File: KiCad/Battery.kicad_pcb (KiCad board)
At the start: 2 copper layers, 19 x 29 mm, 26 parts, among them J1 Connector, J2 USB-C, J3 DC, Q1 RN1701, U1 ESP32-WROOM-32, U2 FT231XQ, U3 NX6020CAKS

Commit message: Tweak regulater
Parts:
- Reg1: footprint RevK:RegulatorBlock2 -> RevK:RegulatorBlock

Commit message: Tweak
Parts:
- moved R7 0.22 mm to (127.5, 110.4)

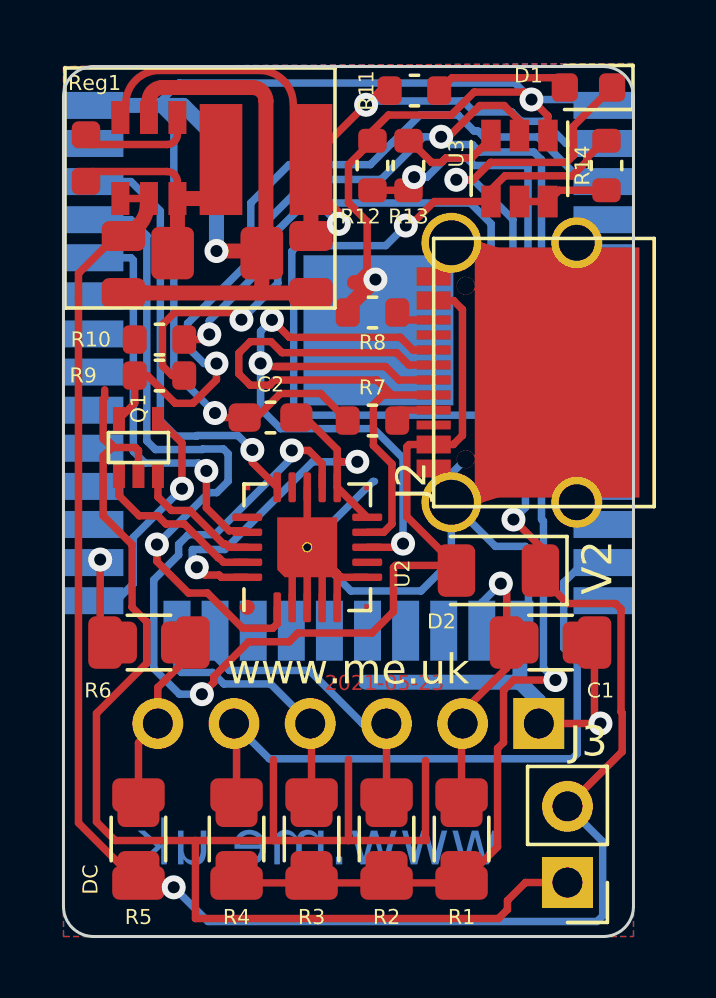
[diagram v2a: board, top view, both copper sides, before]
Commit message: Added BCD_Charger
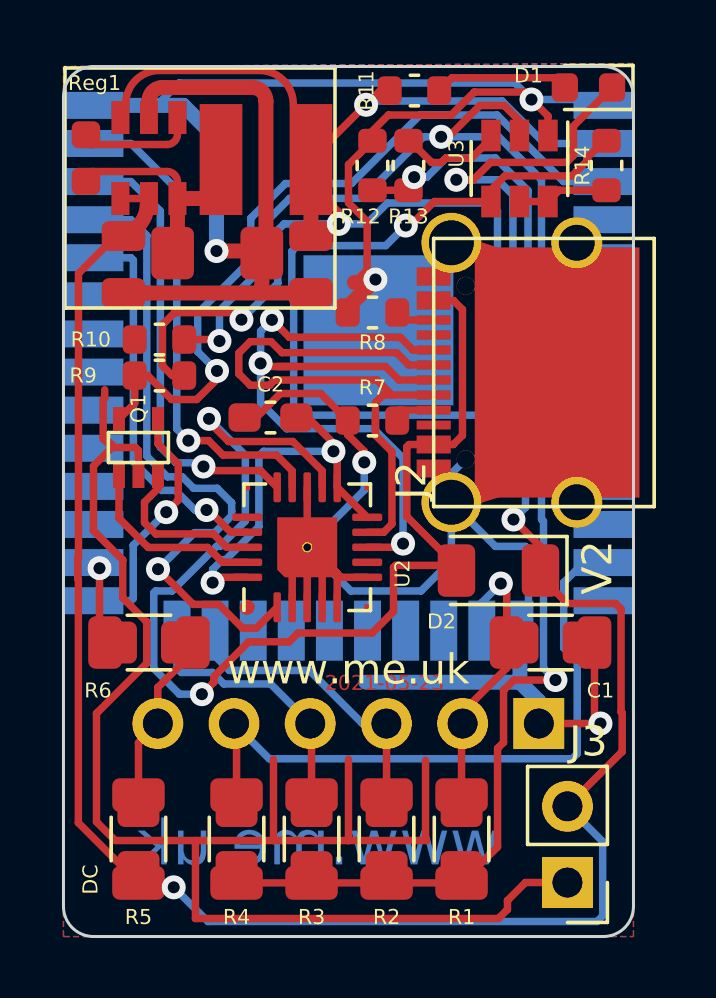
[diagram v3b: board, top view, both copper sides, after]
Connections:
- net CBUS renamed VBUS_SENSE
- U1 pad 37: Net-(U1-Pad37) -> BCD_CHARGER
- U2 pad 14: Net-(U2-Pad14) -> BCD_CHARGER
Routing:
- net BCD_CHARGER: track 0.00 -> 16.4 mm, vias 0 -> 1
- net GND: track 166.2 -> 156.4 mm
- net VBUS: track 37.2 -> 41.1 mm
- net USB3.3: track 14.8 -> 13.5 mm
- net GPIO0: track 4.37 -> 5.50 mm
- net +3V3: track 64.9 -> 63.9 mm
- net Net-(Q1-Pad5): track 26.4 -> 25.5 mm
- net I: track 13.4 -> 12.9 mm

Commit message: USB present is powered CBUS pin
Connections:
- net BCD_CHARGER renamed CHARGER
- net VBUS_SENSE renamed USB

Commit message: Update documentation
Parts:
- C2: footprint Capacitor_SMD:C_0603_1608Metric_Pad1.08x0.95mm_HandSolder -> RevK:C_0603
- moved R7 0.05 mm to (127.5, 110.3)
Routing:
- net GND: track 156.4 -> 158.6 mm
- net USB3.3: track 13.5 -> 12.4 mm
- net O: track 21.5 -> 22.3 mm
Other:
- board text added: "2021-05-25"
- board text added: "V3"
- board text removed: "V2"

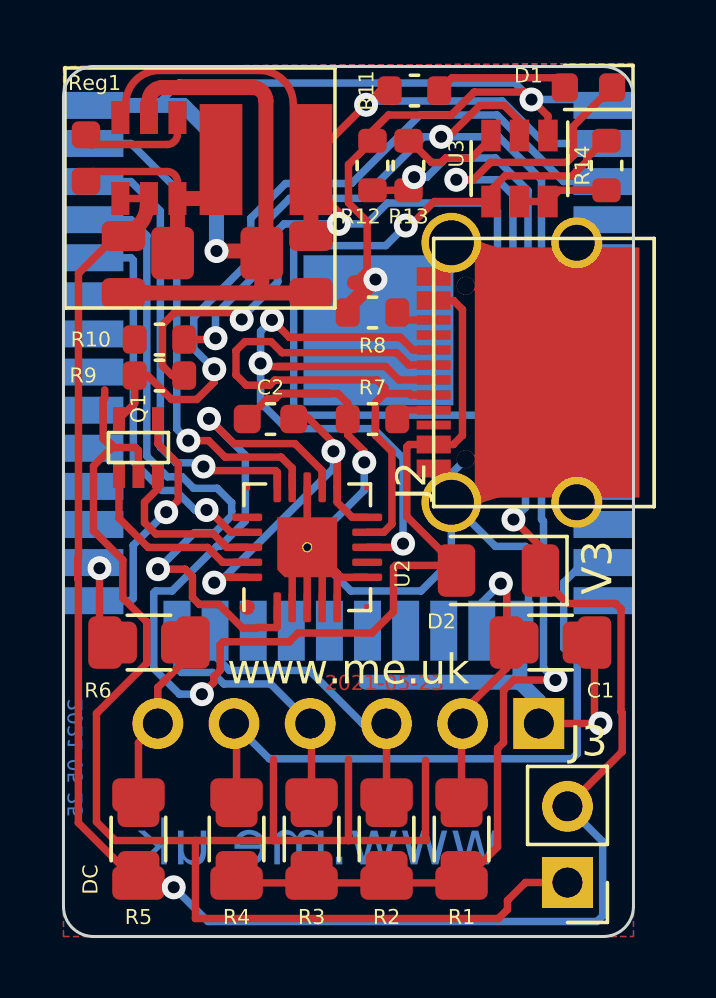
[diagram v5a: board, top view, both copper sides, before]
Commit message: Wrong footprint FFS
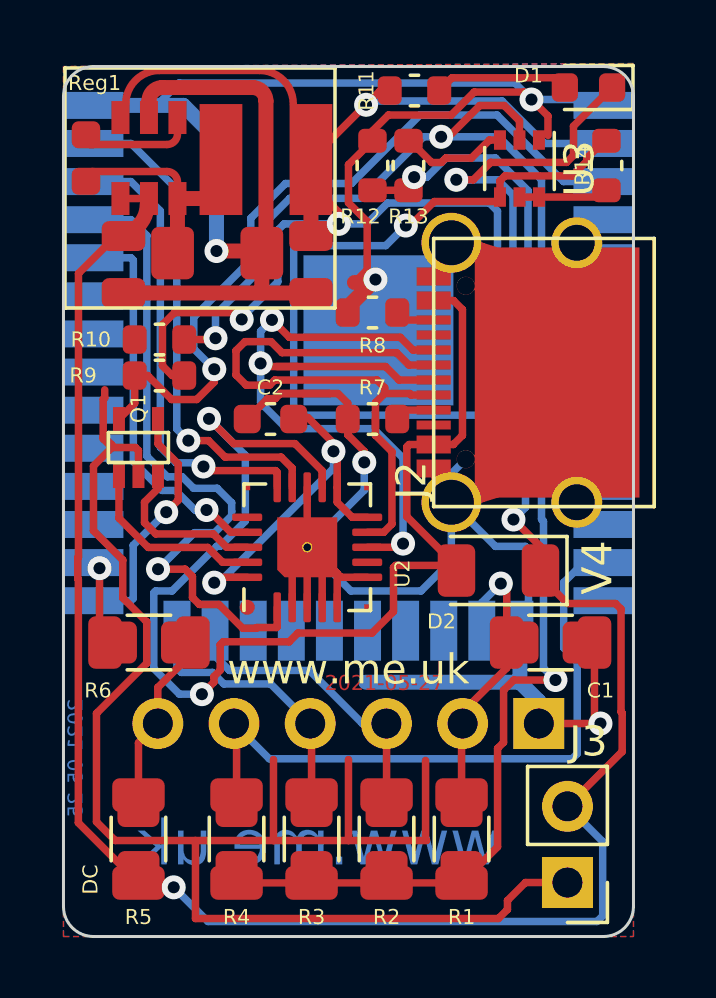
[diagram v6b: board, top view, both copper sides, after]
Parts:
- U3: footprint Package_TO_SOT_SMD:SOT-23-6 -> Package_TO_SOT_SMD:SOT-363_SC-70-6
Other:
- board text added: "2021-05-27"
- board text added: "V4"
- board text removed: "2021-05-23"
- board text removed: "V3"
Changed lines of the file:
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@@
     (thickness 1.6)
     (drawings 34)
-    (tracks 527)
+    (tracks 529)
     (zones 0)
     (modules 26)
@@
   (title_block
     (title "Generic ESP32 (battery)")
-    (date 2021-05-25)
-    (rev 3)
+    (date 2021-05-27)
+    (rev 4)
     (comment 1 www.me.uk)
     (comment 2 @TheRealRevK)
   )
   (layers
-    (0 F.Cu signal hide)
-    (31 B.Cu signal hide)
+    (0 F.Cu signal)
+    (31 B.Cu signal)
     (32 B.Adhes user hide)
     (33 F.Adhes user hide)
     (34 B.Paste user hide)
     (35 F.Paste user hide)
-    (36 B.SilkS user hide)
-    (37 F.SilkS user hide)
+    (36 B.SilkS user)
+    (37 F.SilkS user)
     (38 B.Mask user hide)
     (39 F.Mask user hide)
@@
     (add_net VBUS)
   )
+  (module Package_TO_SOT_SMD:SOT-363_SC-70-6 (layer F.Cu)
+    (at 132.4 102 270)
+    (descr "SOT-363, SC-70-6")
+    (tags "SOT-363 SC-70-6")
+    (attr smd)
+    (fp_text reference U3 (at 0 -2 90) (layer F.SilkS)
+      (effects (font (size 1 1) (thickness 0.15)))
+    )
+    (fp_text value NX6020CAKS (at 0 2 270) (layer F.Fab)
+      (effects (font (size 1 1) (thickness 0.15)))
+    )
+    (fp_line (start -0.175 -1.1) (end -0.675 -0.6) (layer F.Fab) (width 0.1))
+    (fp_line (start 0.675 1.1) (end -0.675 1.1) (layer F.Fab) (width 0.1))
+    (fp_line (start 0.675 -1.1) (end 0.675 1.1) (layer F.Fab) (width 0.1))
+    (fp_line (start -1.6 1.4) (end 1.6 1.4) (layer F.CrtYd) (width 0.05))
+    (fp_line (start -0.675 -0.6) (end -0.675 1.1) (layer F.Fab) (width 0.1))
+    (fp_line (start 0.675 -1.1) (end -0.175 -1.1) (layer F.Fab) (width 0.1))
+    (fp_line (start -1.6 -1.4) (end 1.6 -1.4) (layer F.CrtYd) (width 0.05))
+    (fp_line (start -1.6 -1.4) (end -1.6 1.4) (layer F.CrtYd) (width 0.05))
+    (fp_line (start 1.6 1.4) (end 1.6 -1.4) (layer F.CrtYd) (width 0.05))
+    (fp_line (start -0.7 1.16) (end 0.7 1.16) (layer F.SilkS) (width 0.12))
+    (fp_line (start 0.7 -1.16) (end -1.2 -1.16) (layer F.SilkS) (width 0.12))
+    (fp_text user %R (at 0 0) (layer F.Fab)
+      (effects (font (size 0.5 0.5) (thickness 0.075)))
+    )
+    (pad 6 smd rect (at 0.95 -0.65 270) (size 0.65 0.4) (layers F.Cu F.Paste F.Mask)
+      (net 47 "Net-(R14-Pad1)"))
+    (pad 4 smd rect (at 0.95 0.65 270) (size 0.65 0.4) (layers F.Cu F.Paste F.Mask)
+      (net 41 DC))
+    (pad 2 smd rect (at -0.95 0 270) (size 0.65 0.4) (layers F.Cu F.Paste F.Mask)
+      (net 45 ADCON))
+    (pad 5 smd rect (at 0.95 0 270) (size 0.65 0.4) (layers F.Cu F.Paste F.Mask)
+      (net 47 "Net-(R14-Pad1)"))
+    (pad 3 smd rect (at -0.95 0.65 270) (size 0.65 0.4) (layers F.Cu F.Paste F.Mask)
+      (net 44 "Net-(R12-Pad1)"))
+    (pad 1 smd rect (at -0.95 -0.65 270) (size 0.65 0.4) (layers F.Cu F.Paste F.Mask)
+      (net 2 GND))
+    (model ${KISYS3DMOD}/Package_TO_SOT_SMD.3dshapes/SOT-363_SC-70-6.wrl
+      (at (xyz 0 0 0))
+      (scale (xyz 1 1 1))
+      (rotate (xyz 0 0 0))
+    )
+  )
   (module RevK:C_0603 (layer F.Cu)
     (at 124.1 110.35 180)
@@
     (model ${KISYS3DMOD}/Diode_SMD.3dshapes/D_1206_3216Metric.wrl
       (offset (xyz 0.275 -2.5 0))
-      (scale (xyz 1 1 1))
-      (rotate (xyz 0 0 0))
-    )
-  )
-  (module Package_TO_SOT_SMD:SOT-23-6 (layer F.Cu)
-    (at 132.4 102 270)
-    (descr "6-pin SOT-23 package")
-    (tags SOT-23-6)
-    (attr smd)
-    (fp_text reference U3 (at -0.5 2.1 90) (layer F.SilkS)
-      (effects (font (size 0.5 0.5) (thickness 0.08)))
-    )
-    (fp_text value NX6020CAKS (at 1.5 1.7 180) (layer F.Fab)
-      (effects (font (size 0.5 0.5) (thickness 0.08)) (justify left))
-    )
-    (fp_line (start -0.9 1.61) (end 0.9 1.61) (layer F.SilkS) (width 0.12))
-    (fp_line (start 0.9 -1.61) (end -1.55 -1.61) (layer F.SilkS) (width 0.12))
-    (fp_line (start 1.9 -1.8) (end -1.9 -1.8) (layer F.CrtYd) (width 0.05))
-    (fp_line (start 1.9 1.8) (end 1.9 -1.8) (layer F.CrtYd) (width 0.05))
-    (fp_line (start -1.9 1.8) (end 1.9 1.8) (layer F.CrtYd) (width 0.05))
-    (fp_line (start -1.9 -1.8) (end -1.9 1.8) (layer F.CrtYd) (width 0.05))
-    (fp_line (start -0.9 -0.9) (end -0.25 -1.55) (layer F.Fab) (width 0.1))
-    (fp_line (start 0.9 -1.55) (end -0.25 -1.55) (layer F.Fab) (width 0.1))
-    (fp_line (start -0.9 -0.9) (end -0.9 1.55) (layer F.Fab) (width 0.1))
-    (fp_line (start 0.9 1.55) (end -0.9 1.55) (layer F.Fab) (width 0.1))
-    (fp_line (start 0.9 -1.55) (end 0.9 1.55) (layer F.Fab) (width 0.1))
-    (fp_text user %R (at -1.5 1.15) (layer F.Fab)
-      (effects (font (size 0.5 0.5) (thickness 0.075)))
-    )
-    (pad 5 smd rect (at 1.1 0 270) (size 1.06 0.65) (layers F.Cu F.Paste F.Mask)
-      (net 47 "Net-(R14-Pad1)"))
-    (pad 6 smd rect (at 1.1 -0.95 270) (size 1.06 0.65) (layers F.Cu F.Paste F.Mask)
-      (net 47 "Net-(R14-Pad1)"))
-    (pad 4 smd rect (at 1.1 0.95 270) (size 1.06 0.65) (layers F.Cu F.Paste F.Mask)
-      (net 41 DC))
-    (pad 3 smd rect (at -1.1 0.95 270) (size 1.06 0.65) (layers F.Cu F.Paste F.Mask)
-      (net 44 "Net-(R12-Pad1)"))
-    (pad 2 smd rect (at -1.1 0 270) (size 1.06 0.65) (layers F.Cu F.Paste F.Mask)
-      (net 45 ADCON))
-    (pad 1 smd rect (at -1.1 -0.95 270) (size 1.06 0.65) (layers F.Cu F.Paste F.Mask)
-      (net 2 GND))
-    (model ${KISYS3DMOD}/Package_TO_SOT_SMD.3dshapes/SOT-23-6.wrl
-      (at (xyz 0 0 0))
       (scale (xyz 1 1 1))
       (rotate (xyz 0 0 0))
@@
     (effects (font (size 0.5 0.5) (thickness 0.08)))
   )
-  (gr_text 2021-05-23 (at 127.9 119.15) (layer F.Cu)
+  (gr_text 2021-05-27 (at 127.9 119.15) (layer F.Cu)
     (effects (font (size 0.5 0.5) (thickness 0.08)))
   )
@@
     (effects (font (size 1 1) (thickness 0.15)))
   )
-  (gr_text V3 (at 135 115.3 90) (layer F.SilkS)
+  (gr_text V4 (at 135 115.3 90) (layer F.SilkS)
     (effects (font (size 1 1) (thickness 0.15)))
   )
@@
   (segment (start 134.650009 101.749991) (end 134.155001 102.244999) (width 0.25) (layer F.Cu) (net 41))
   (segment (start 134.155001 102.244999) (end 131.914999 102.244999) (width 0.25) (layer F.Cu) (net 41))
-  (segment (start 131.45 102.709998) (end 131.45 103.1) (width 0.25) (layer F.Cu) (net 41))
-  (segment (start 131.914999 102.244999) (end 131.45 102.709998) (width 0.25) (layer F.Cu) (net 41))
   (segment (start 119.7 125.8125) (end 120.727873 125.8125) (width 0.25) (layer F.Cu) (net 41))
   (via (at 120.87499 125.959617) (size 0.8) (drill 0.4) (layers F.Cu B.Cu) (net 41))
@@
   (segment (start 129.560684 103.1) (end 128.75922 103.901463) (width 0.25) (layer F.Cu) (net 41))
   (via (at 128.611362 103.901463) (size 0.8) (drill 0.4) (layers F.Cu B.Cu) (net 41))
-  (segment (start 131.45 103.1) (end 129.560684 103.1) (width 0.25) (layer F.Cu) (net 41))
   (segment (start 119.1 103) (end 120.05 103) (width 0.25) (layer F.Cu) (net 41))
   (segment (start 119.1375 125.25) (end 119.7 125.8125) (width 0.25) (layer F.Cu) (net 41))
@@
   (segment (start 132.321408 110.221408) (end 132.6 110.5) (width 0.25) (layer B.Cu) (net 41))
   (segment (start 132.599999 113.300001) (end 132.2 113.7) (width 0.25) (layer B.Cu) (net 41))
+  (segment (start 131.75 102.409998) (end 131.75 102.95) (width 0.25) (layer F.Cu) (net 41))
+  (segment (start 131.914999 102.244999) (end 131.75 102.409998) (width 0.25) (layer F.Cu) (net 41))
+  (segment (start 131.6 103.1) (end 131.75 102.95) (width 0.25) (layer F.Cu) (net 41))
+  (segment (start 129.560684 103.1) (end 131.6 103.1) (width 0.25) (layer F.Cu) (net 41))
   (segment (start 119.05 110.35) (end 119.575 109.825) (width 0.25) (layer F.Cu) (net 42) (status 10))
   (segment (start 119.575 109.825) (end 119.575 108.9) (width 0.25) (layer F.Cu) (net 42) (status 20))
@@
   (segment (start 128.7 101.075) (end 129.075 101.075) (width 0.25) (layer F.Cu) (net 44))
   (segment (start 129.946034 101.649988) (end 129.796022 101.8) (width 0.25) (layer F.Cu) (net 44))
-  (segment (start 131.55 100.9) (end 130.800012 101.649988) (width 0.25) (layer F.Cu) (net 44))
   (segment (start 128.750086 101.075) (end 128.7 101.075) (width 0.25) (layer F.Cu) (net 44))
   (segment (start 130.800012 101.649988) (end 129.946034 101.649988) (width 0.25) (layer F.Cu) (net 44))
   (segment (start 129.796022 101.8) (end 129.475086 101.8) (width 0.25) (layer F.Cu) (net 44))
   (segment (start 129.475086 101.8) (end 128.750086 101.075) (width 0.25) (layer F.Cu) (net 44))
+  (segment (start 131.4 101.05) (end 130.800012 101.649988) (width 0.25) (layer F.Cu) (net 44))
+  (segment (start 131.75 101.05) (end 131.4 101.05) (width 0.25) (layer F.Cu) (net 44))
   (segment (start 131.890002 99.9) (end 132.4 100.409998) (width 0.25) (layer F.Cu) (net 45))
   (via (at 129.789783 100.942016) (size 0.8) (drill 0.4) (layers F.Cu B.Cu) (net 45))
@@
   (segment (start 134.437824 110.055) (end 132.684988 108.302164) (width 0.25) (layer B.Cu) (net 46))
   (segment (start 135.2 110.055) (end 134.437824 110.055) (width 0.25) (layer B.Cu) (net 46))
-  (segment (start 133.725 102.725) (end 133.35 103.1) (width 0.25) (layer F.Cu) (net 47))
-  (segment (start 135.3 102.725) (end 133.725 102.725) (width 0.25) (layer F.Cu) (net 47))
-  (segment (start 133.35 103.1) (end 132.4 103.1) (width 0.25) (layer F.Cu) (net 47))
+  (segment (start 132.4 102.95) (end 133.05 102.95) (width 0.25) (layer F.Cu) (net 47))
+  (segment (start 135.075 102.95) (end 135.3 102.725) (width 0.25) (layer F.Cu) (net 47))
+  (segment (start 133.05 102.95) (end 135.075 102.95) (width 0.25) (layer F.Cu) (net 47))
   (segment (start 120.976367 110.682743) (end 121.363164 111.06954) (width 0.25) (layer B.Cu) (net 48))
   (segment (start 119.45 101.165) (end 120.976367 102.691367) (width 0.25) (layer B.Cu) (net 48))

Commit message: Fix close via
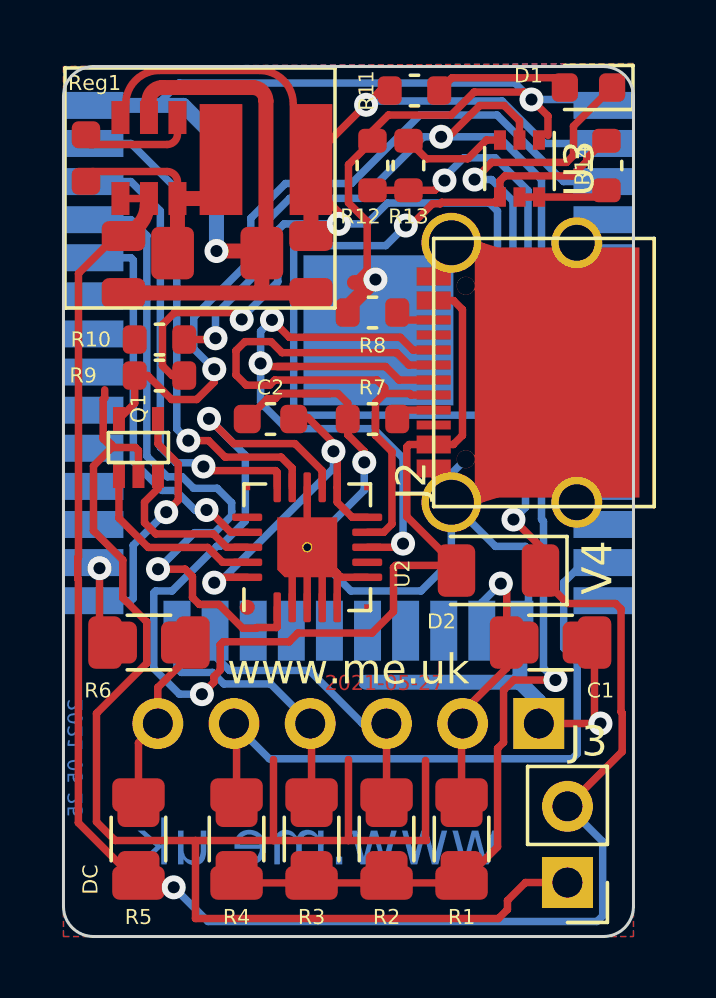
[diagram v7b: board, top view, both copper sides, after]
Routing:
- net Net-(D1-Pad1): track 19.6 -> 18.2 mm

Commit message: Tidy drawing
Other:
- board text added: "22"
- board text added: "23"
- board text added: "25"
- board text added: "32"
- board text added: "33"
